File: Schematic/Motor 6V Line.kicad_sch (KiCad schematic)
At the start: 0 parts

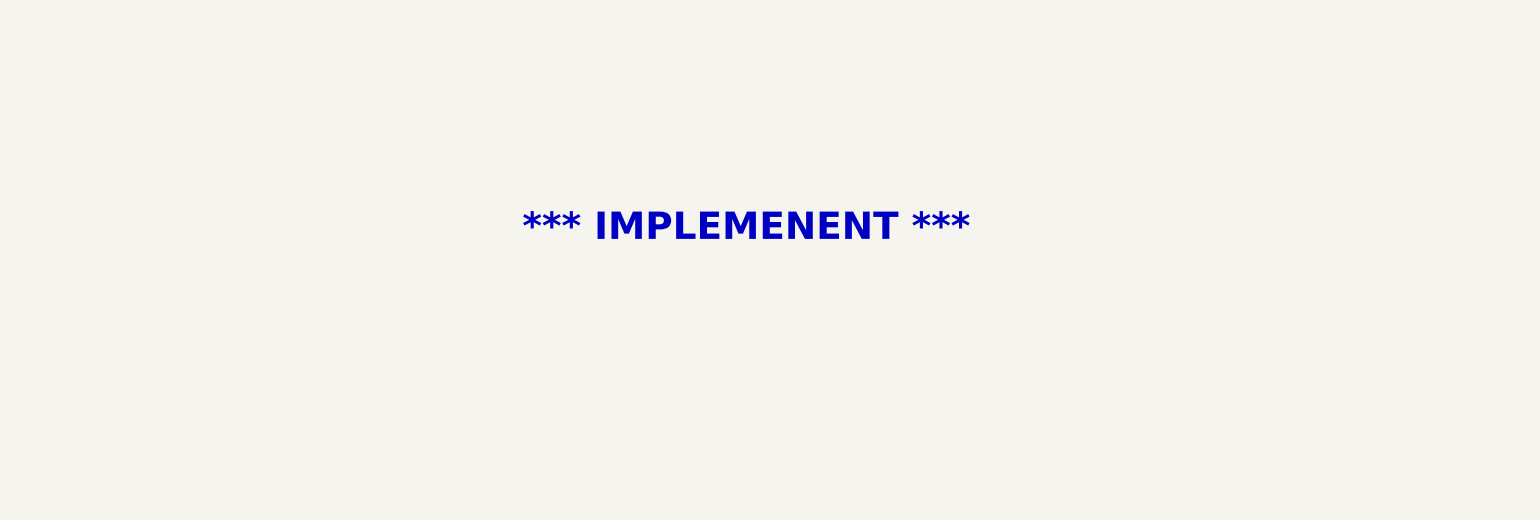
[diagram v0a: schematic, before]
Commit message: Added 6V Line
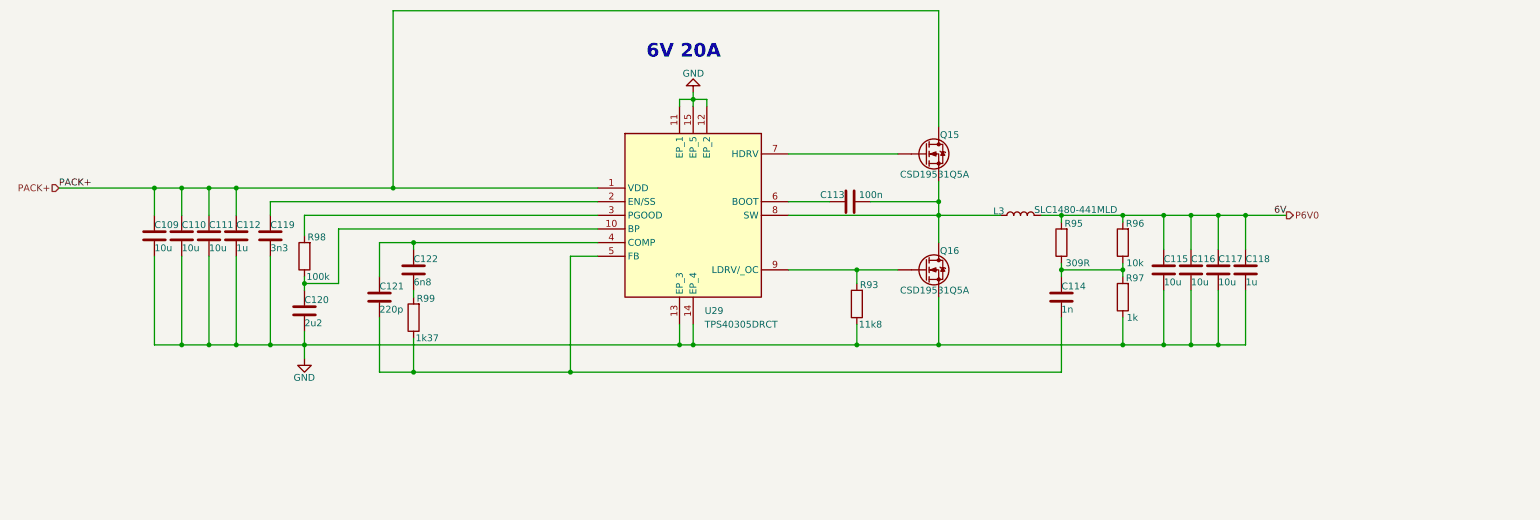
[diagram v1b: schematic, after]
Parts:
- added C109, C110, C111, C115, C116, C117: 10u, symbol Device:C
- added C112, C118: 1u, symbol Device:C
- added C113: 100n, symbol Device:C
- added C114: 1n, symbol Device:C
- added C119: 3n3, symbol Device:C
- added C120: 2u2, symbol Device:C
- added C121: 220p, symbol Device:C
- added C122: 6n8, symbol Device:C
- added L3: SLC1480-441MLD, SLC1480441MLD, symbol SLC1480-441MLD:SLC1480-441MLD
- added Q15, Q16: CSD19531Q5A, symbol Transistor_FET:CSD19531Q5A
- added R93: 11k8, symbol Device:R
- added R95: 309R, symbol Device:R
- added R96: 10k, symbol Device:R
- added R97: 1k, symbol Device:R
- added R98: 100k, symbol Device:R
- added R99: 1k37, symbol Device:R
- added U29: TPS40305DRCT, TPS40305DRCT, symbol TPS40305DRCT:TPS40305DRCT
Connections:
- new net: Q16.4 (G), R93.2, U29.9 (LDRV/_OC)
- new net: C113.2, L3.1, Q15.1 (S), Q15.2 (S), Q15.3 (S), Q16.5 (D), U29.8 (SW)
- new net: C120.1, R98.1, U29.10 (BP)
- new net: C119.1, U29.2 (EN/SS)
- new net: R98.2, U29.3 (PGOOD)
- new net: C121.1, C122.1, U29.4 (COMP)
- new net: C114.2, C121.2, R99.1, U29.5 (FB)
- new net: C113.1, U29.6 (BOOT)
- new net: Q15.4 (G), U29.7 (HDRV)
- new net: C122.2, R99.2
- new net: C114.1, R95.1, R96.1, R97.2
- new net GND: C109.2, C110.2, C111.2, C112.2, C115.2, C116.2, C117.2, C118.2, C119.2, C120.2, Q16.1 (S), Q16.2 (S), Q16.3 (S), R93.1, R97.1, U29.11 (EP_1), U29.12 (EP_2), U29.13 (EP_3), U29.14 (EP_4), U29.15 (EP_5)
- new net P6V0: C115.1, C116.1, C117.1, C118.1, L3.2, R95.2, R96.2
- new net PACK+: C109.1, C110.1, C111.1, C112.1, Q15.5 (D), U29.1 (VDD)
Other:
- note added: "6V 20A"
- note removed: "*** IMPLEMENENT ***"

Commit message: bom progress
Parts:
- added C123, C124, C125, C126, C127, C128: 10u, symbol Device:C
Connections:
- net GND: now also C123.2, C124.2, C125.2, C126.2, C127.2, C128.2
- net P6V0: now also C123.1, C124.1, C125.1
- net PACK+: now also C126.1, C127.1, C128.1
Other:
- note added: "I_RMS(cin) = I_OUT * sqrt(D * (1 - D)) I_RMS(cin) = 20 A * sqrt(0.5 * (1 - 0.5)) = 10 A"
- note added: "I_RMS(cout) = I_RIPPLE / sqrt(12) I_RIPPLE = ((V_IN_max - V_OUT) / L) * (V_OUT / V_IN_max) * (1 / f_SW) I_RIPPLE = ((12.6 V - 6 V) / 440 nH) * (6 V / 12.6 V) * (1 / 1.2 MHz) = 5.95 A"
- moved on the sheet: C109, C110, C111, C112, C113, C114, C115, C116, C117, C118, C119, C120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

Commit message: 100n cap
100n cap bom
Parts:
- C113: footprint (none) -> CL10B104MB8NNNC:CAPC1608X90N; Link (none) -> https://mou.sr/3JWJm45; Manufacturer Part Number (none) -> CL10B104MB8NNNC; Price per Unit (none) -> 0.10; Supplier (none) -> Mouser; Supplier Part Number (none) -> 187-CL10B104MB8NNNC
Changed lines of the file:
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@@
 			)
 		)
-		(property "Footprint" ""
+		(property "Footprint" "CL10B104MB8NNNC:CAPC1608X90N"
 			(at 176.53 98.0948 0)
 			(effects
@@
 			)
 		)
-		(property "Link" ""
-			(at 172.72 99.06 0)
-			(effects
-				(font
-					(size 1.27 1.27)
-				)
-				(hide yes)
-			)
-		)
-		(property "Manufacturer Part Number" ""
-			(at 172.72 99.06 0)
-			(effects
-				(font
-					(size 1.27 1.27)
-				)
-				(hide yes)
-			)
-		)
-		(property "Price per Unit" ""
-			(at 172.72 99.06 0)
-			(effects
-				(font
-					(size 1.27 1.27)
-				)
-				(hide yes)
-			)
-		)
-		(property "Supplier" ""
-			(at 172.72 99.06 0)
-			(effects
-				(font
-					(size 1.27 1.27)
-				)
-				(hide yes)
-			)
-		)
-		(property "Supplier Part Number" ""
-			(at 172.72 99.06 0)
-			(effects
+		(property "Link" "https://mou.sr/3JWJm45"
+			(at 172.72 99.06 0)
+			(effects
+				(font
+					(size 1.27 1.27)
+				)
+				(hide yes)
+			)
+		)
+		(property "Manufacturer Part Number" "CL10B104MB8NNNC"
+			(at 172.72 99.06 0)
+			(effects
+				(font
+					(size 1.27 1.27)
+				)
+				(hide yes)
+			)
+		)
+		(property "Price per Unit" "0.10"
+			(at 172.72 99.06 0)
+			(effects
+				(font
+					(size 1.27 1.27)
+				)
+				(hide yes)
+			)
+		)
+		(property "Supplier" "Mouser"
+			(at 172.72 99.06 0)
+			(effects
+				(font
+					(size 1.27 1.27)
+				)
+				(hide yes)
+			)
+		)
+		(property "Supplier Part Number" "187-CL10B104MB8NNNC "
+			(at 172.72 99.06 0)
+			(effects

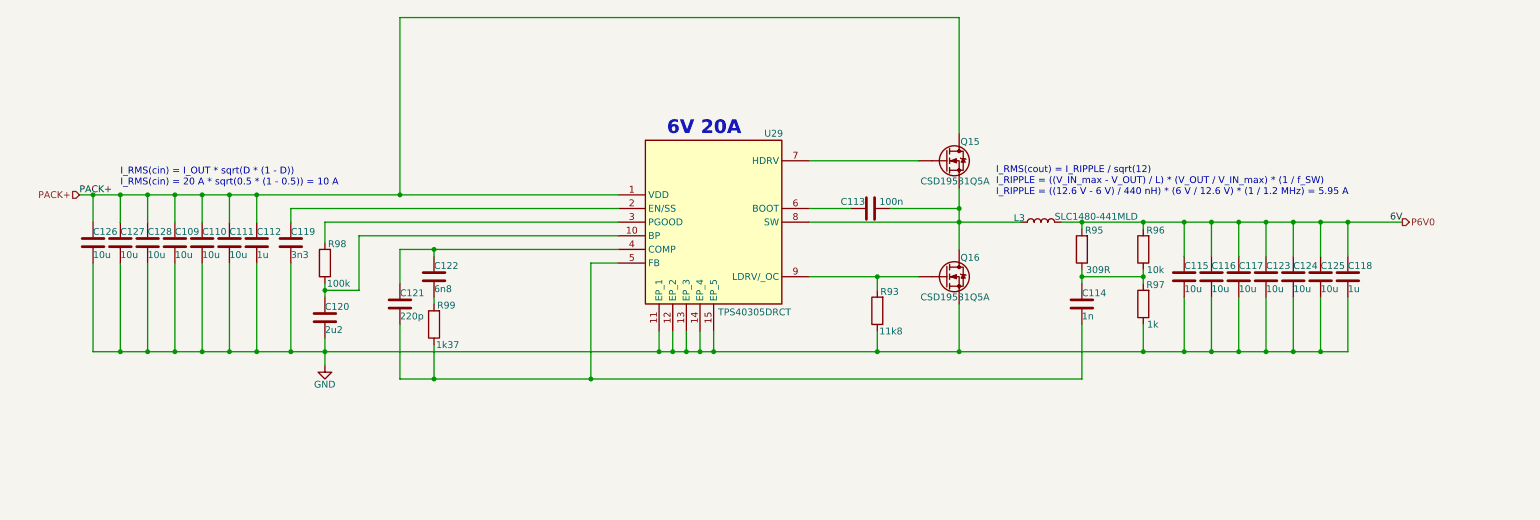
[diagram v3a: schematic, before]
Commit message: added test points and fet
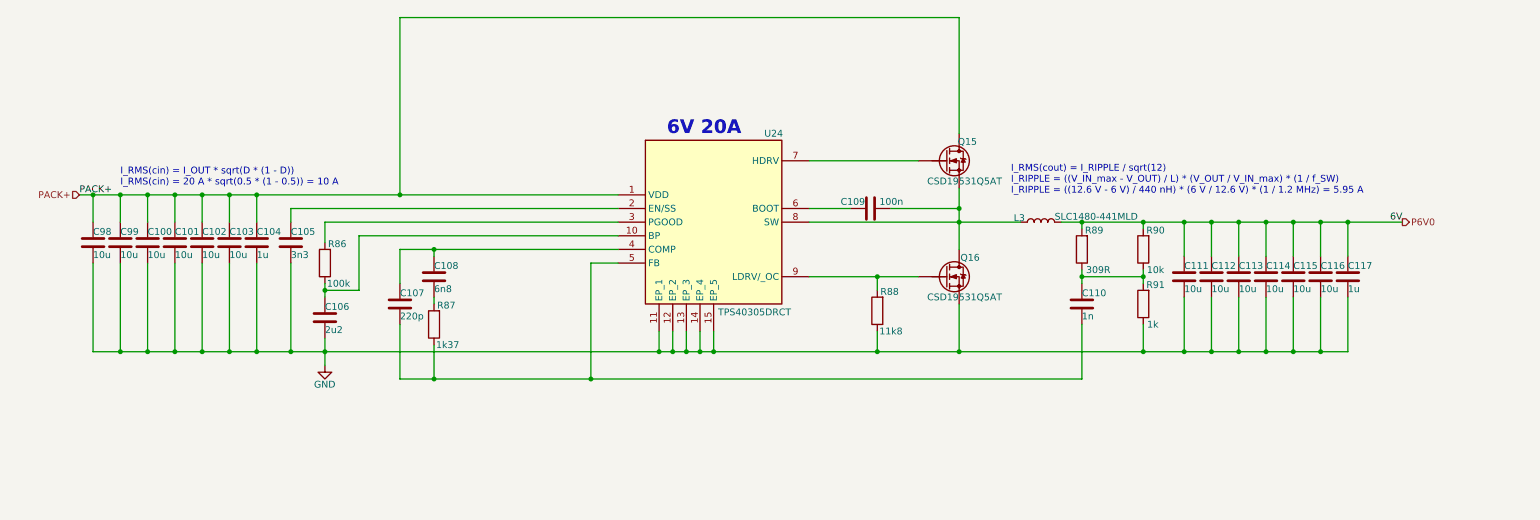
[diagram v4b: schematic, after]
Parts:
- removed Q15, Q16: CSD19531Q5A, symbol Transistor_FET:CSD19531Q5A
- added Q15, Q16: CSD19531Q5AT, CSD19531Q5AT, symbol CSD19531Q5AT:CSD19531Q5AT
- C109: renamed from C113; footprint CL10B104MB8NNNC:CAPC1608X90N -> Capacitor_SMD:C_0603_1608Metric_Pad1.08x0.95mm_HandSolder
- renumbered C128 to C100, C109 to C101, C110 to C102, C111 to C103, C112 to C104, C119 to C105, C120 to C106, C121 to C107, C122 to C108, C114 to C110, C115 to C111, C116 to C112, C117 to C113, C123 to C114, C124 to C115, C125 to C116, C118 to C117, C126 to C98, C127 to C99, R98 to R86, R99 to R87, R93 to R88, R95 to R89, R96 to R90, R97 to R91, U29 to U24
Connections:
- net GND: now also Q16.1 (S), Q16.2 (S), Q16.3 (S)
- net PACK+: now also Q15.5 (D), Q15.6 (D), Q15.7 (D), Q15.8 (D), Q15.9 (D)
- net at R88.2, U24.9 (LDRV/_OC): now also Q16.4 (G)
- net at C109.2, L3.1, U24.8 (SW): now also Q15.1 (S), Q15.2 (S), Q15.3 (S), Q16.5 (D), Q16.6 (D), Q16.7 (D), Q16.8 (D), Q16.9 (D)
- net at U24.7 (HDRV): now also Q15.4 (G)

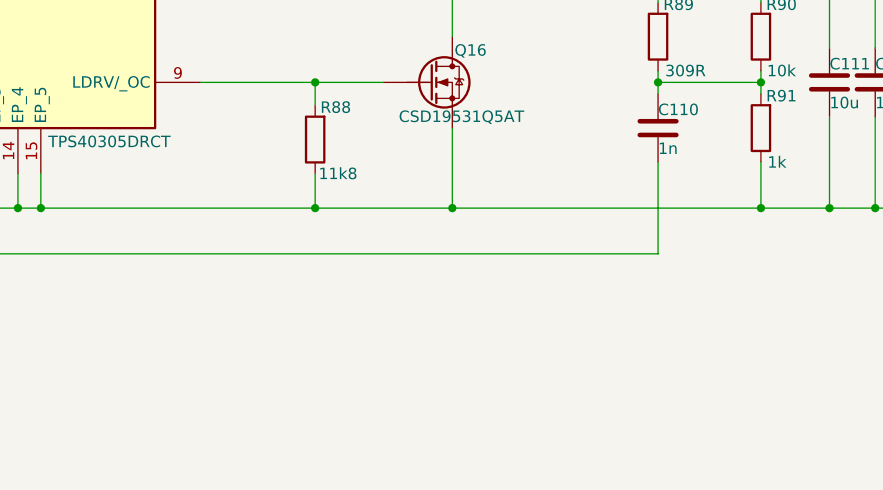
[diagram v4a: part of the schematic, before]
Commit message: More REsistor
16 res down for bom
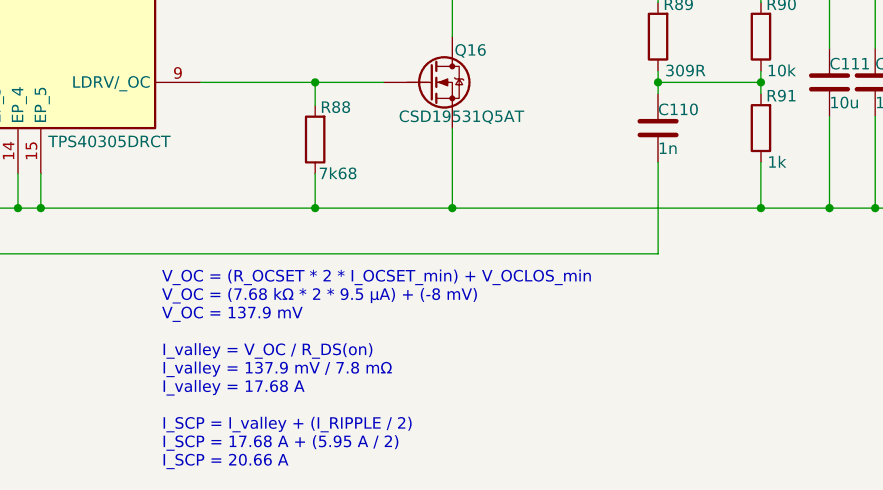
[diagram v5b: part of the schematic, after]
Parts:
- R86: footprint (none) -> Resistor_SMD:R_0603_1608Metric_Pad0.98x0.95mm_HandSolder; Link (none) -> https://mou.sr/4n9UsBp; Manufacturer Part Number (none) -> AC0603FR-7W4K7L; Price per Unit (none) -> 0.10; Supplier (none) -> Mouser; Supplier Part Number (none) -> 603-AC0603FR-7W4K7L
- R87: footprint (none) -> Resistor_SMD:R_0603_1608Metric_Pad0.98x0.95mm_HandSolder; Link (none) -> https://mou.sr/3IjcfqA; Manufacturer Part Number (none) -> RT0603DRE071K37L; Price per Unit (none) -> 0.10; Supplier (none) -> Mouser; Supplier Part Number (none) -> 603-RT0603DRE071K37L
- R88: value 11k8 -> 7k68; footprint (none) -> Resistor_SMD:R_0603_1608Metric_Pad0.98x0.95mm_HandSolder; Link (none) -> https://mou.sr/4pmZ9Jx; Manufacturer Part Number (none) -> RT0603FRE077K68L; Price per Unit (none) -> 0.10; Supplier (none) -> Mouser; Supplier Part Number (none) -> 603-RT0603FRE077K68L
- R89: footprint (none) -> Resistor_SMD:R_0603_1608Metric_Pad0.98x0.95mm_HandSolder; Link (none) -> https://mou.sr/4mbJQRa; Manufacturer Part Number (none) -> ERA-3AEB3090V; Price per Unit (none) -> 0.10; Supplier (none) -> Mouser; Supplier Part Number (none) -> 667-ERA-3AEB3090V
- R90: footprint (none) -> Resistor_SMD:R_0603_1608Metric_Pad0.98x0.95mm_HandSolder; Link (none) -> https://mou.sr/463dpQf; Manufacturer Part Number (none) -> RCA060310K0FKEC; Price per Unit (none) -> 0.10; Supplier (none) -> Mouser; Supplier Part Number (none) -> 71-RCA060310K0FKEC
- R91: footprint (none) -> Resistor_SMD:R_0603_1608Metric_Pad0.98x0.95mm_HandSolder; Link (none) -> https://mou.sr/4pjaV7O; Manufacturer Part Number (none) -> MCT0603MD1001DP500; Price per Unit (none) -> 0.10; Supplier (none) -> Mouser; Supplier Part Number (none) -> 594-MCT0603MD1001DP5
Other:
- note added: "V_OC = (R_OCSET * 2 * I_OCSET_min) + V_OCLOS_min V_OC = (7.68 kΩ * 2 * 9.5 µA) + (-8 mV) V_OC = 137.9 mV I_valley = V_OC / R_DS(on) I_valley = 137.9 mV / 7.8 mΩ I_valley = 17.68 A I_SCP = I_valley + (I_RIPPLE / 2) I_SCP = 17.68 A + (5.95 A / 2) I_SCP = 20.66 A"
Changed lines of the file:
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@@
 	(generator_version "9.0")
 	(paper "A4")
+	(text "V_OC = (R_OCSET * 2 * I_OCSET_min) + V_OCLOS_min\nV_OC = (7.68 kΩ * 2 * 9.5 µA) + (-8 mV)\nV_OC = 137.9 mV\n\nI_valley = V_OC / R_DS(on)\nI_valley = 137.9 mV / 7.8 mΩ\nI_valley = 17.68 A\n\nI_SCP = I_valley + (I_RIPPLE / 2)\nI_SCP = 17.68 A + (5.95 A / 2)\nI_SCP = 20.66 A"
+		(exclude_from_sim no)
+		(at 156.972 143.764 0)
+		(effects
+			(font
+				(size 1.27 1.27)
+			)
+			(justify left)
+		)
+	)
 	(text "6V 20A"
 		(exclude_from_sim no)
@@
 			)
 		)
-		(property "Footprint" ""
+		(property "Footprint" "Resistor_SMD:R_0603_1608Metric_Pad0.98x0.95mm_HandSolder"
 			(at 72.898 109.22 90)
 			(effects
@@
 			)
 		)
-		(property "Link" ""
+		(property "Link" "https://mou.sr/4n9UsBp"
 			(at 71.12 109.22 0)
 			(effects
@@
 			)
 		)
-		(property "Manufacturer Part Number" ""
+		(property "Manufacturer Part Number" "AC0603FR-7W4K7L"
 			(at 71.12 109.22 0)
 			(effects
@@
 			)
 		)
-		(property "Price per Unit" ""
+		(property "Price per Unit" "0.10"
 			(at 71.12 109.22 0)
 			(effects
@@
 			)
 		)
+		(property "Supplier" "Mouser"
+			(at 71.12 109.22 0)
+			(effects
+				(font
+					(size 1.27 1.27)
+				)
+				(hide yes)
+			)
+		)
+		(property "Supplier Part Number" "603-AC0603FR-7W4K7L"
+			(at 71.12 109.22 0)
+			(effects
+				(font
+					(size 1.27 1.27)
+				)
+				(hide yes)
+			)
+		)
 		(pin "1"
 		)
@@
 			)
 		)
-		(property "Value" "11k8"
+		(property "Value" "7k68"
 			(at 176.53 121.92 0)
 			(effects
@@
 			)
 		)
-		(property "Footprint" ""
+		(property "Footprint" "Resistor_SMD:R_0603_1608Metric_Pad0.98x0.95mm_HandSolder"
 			(at 175.768 118.11 90)
 			(effects
@@
 			)
 		)
-		(property "Link" ""
+		(property "Link" "https://mou.sr/4pmZ9Jx"
 			(at 173.99 118.11 0)
 			(effects
@@
 			)
 		)
-		(property "Manufacturer Part Number" ""
+		(property "Manufacturer Part Number" "RT0603FRE077K68L"
 			(at 173.99 118.11 0)
 			(effects
@@
 			)
 		)
-		(property "Price per Unit" ""
+		(property "Price per Unit" "0.10"
 			(at 173.99 118.11 0)
 			(effects
@@
 			)
 		)
+		(property "Supplier" "Mouser"
+			(at 173.99 118.11 0)
+			(effects
+				(font
+					(size 1.27 1.27)
+				)
+				(hide yes)
+			)
+		)
+		(property "Supplier Part Number" "603-RT0603FRE077K68L"
+			(at 173.99 118.11 0)
+			(effects
+				(font
+					(size 1.27 1.27)
+				)
+				(hide yes)
+			)
+		)
 		(pin "1"
 		)
@@
 			)
 		)
-		(property "Footprint" ""
+		(property "Footprint" "Resistor_SMD:R_0603_1608Metric_Pad0.98x0.95mm_HandSolder"
 			(at 93.218 120.65 90)
 			(effects
@@
 			)
 		)
-		(property "Link" ""
+		(property "Link" "https://mou.sr/3IjcfqA"
 			(at 91.44 120.65 0)
 			(effects
@@
 			)
 		)
-		(property "Manufacturer Part Number" ""
+		(property "Manufacturer Part Number" "RT0603DRE071K37L "
 			(at 91.44 120.65 0)
 			(effects
@@
 			)
 		)
-		(property "Price per Unit" ""
+		(property "Price per Unit" "0.10"
 			(at 91.44 120.65 0)
 			(effects
@@
 			)
 		)
+		(property "Supplier" "Mouser"
+			(at 91.44 120.65 0)
+			(effects
+				(font
+					(size 1.27 1.27)
+				)
+				(hide yes)
+			)
+		)
+		(property "Supplier Part Number" "603-RT0603DRE071K37L"
+			(at 91.44 120.65 0)
+			(effects
+				(font
+					(size 1.27 1.27)
+				)
+				(hide yes)
+			)
+		)
 		(pin "1"
 		)
@@
 			)
 		)
-		(property "Footprint" ""
+		(property "Footprint" "Resistor_SMD:R_0603_1608Metric_Pad0.98x0.95mm_HandSolder"
 			(at 225.298 116.84 90)
 			(effects
@@
 			)
 		)
-		(property "Link" ""
+		(property "Link" "https://mou.sr/4pjaV7O"
 			(at 223.52 116.84 0)
 			(effects
@@
 			)
 		)
-		(property "Manufacturer Part Number" ""
+		(property "Manufacturer Part Number" "MCT0603MD1001DP500 "
 			(at 223.52 116.84 0)
 			(effects
@@
 			)
 		)
-		(property "Price per Unit" ""
+		(property "Price per Unit" "0.10"
 			(at 223.52 116.84 0)
 			(effects
@@
 			)
 		)
+		(property "Supplier" "Mouser"
+			(at 223.52 116.84 0)
+			(effects
+				(font
+					(size 1.27 1.27)
+				)
+				(hide yes)
+			)
+		)
+		(property "Supplier Part Number" "594-MCT0603MD1001DP5 "
+			(at 223.52 116.84 0)
+			(effects
+				(font
+					(size 1.27 1.27)
+				)
+				(hide yes)
+			)
+		)
 		(pin "1"
 		)
@@
 			)
 		)
-		(property "Footprint" ""
+		(property "Footprint" "Resistor_SMD:R_0603_1608Metric_Pad0.98x0.95mm_HandSolder"
 			(at 225.298 106.68 90)
 			(effects
@@
 			)
 		)
-		(property "Link" ""
+		(property "Link" "https://mou.sr/463dpQf"
 			(at 223.52 106.68 0)
 			(effects
@@
 			)
 		)
-		(property "Manufacturer Part Number" ""
+		(property "Manufacturer Part Number" "RCA060310K0FKEC "
 			(at 223.52 106.68 0)
 			(effects
@@
 			)
 		)
-		(property "Price per Unit" ""
+		(property "Price per Unit" "0.10"
 			(at 223.52 106.68 0)
 			(effects
@@
 			)
 		)
+		(property "Supplier" "Mouser"
+			(at 223.52 106.68 0)
+			(effects
+				(font
+					(size 1.27 1.27)
+				)
+				(hide yes)
+			)
+		)
+		(property "Supplier Part Number" "71-RCA060310K0FKEC"
+			(at 223.52 106.68 0)
+			(effects
+				(font
+					(size 1.27 1.27)
+				)
+				(hide yes)
+			)
+		)
 		(pin "1"
 		)
@@
 			)
 		)
-		(property "Footprint" ""
+		(property "Footprint" "Resistor_SMD:R_0603_1608Metric_Pad0.98x0.95mm_HandSolder"
 			(at 213.868 106.68 90)
 			(effects
@@
 			)
 		)
-		(property "Link" ""
+		(property "Link" "https://mou.sr/4mbJQRa"
 			(at 212.09 106.68 0)
 			(effects
@@
 			)
 		)
-		(property "Manufacturer Part Number" ""
+		(property "Manufacturer Part Number" "ERA-3AEB3090V "
 			(at 212.09 106.68 0)
 			(effects
@@
 			)
 		)
-		(property "Price per Unit" ""
+		(property "Price per Unit" "0.10"
 			(at 212.09 106.68 0)
 			(effects
@@
 			(at 212.09 106.68 0)
 			(effects
+				(font
+					(size 1.27 1.27)
+				)
+				(hide yes)
+			)
+		)
+		(property "Supplier" "Mouser"
+			(at 212.09 106.68 0)
+			(effects
+				(font
+					(size 1.27 1.27)
+				)
+				(hide yes)
+			)
+		)
+		(property "Supplier Part Number" "667-ERA-3AEB3090V"
+			(at 212.09 106.68 0)
+			(effects
